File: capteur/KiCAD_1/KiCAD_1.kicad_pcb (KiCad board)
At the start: 2 copper layers, 68.6 x 58.3 mm, 25 parts, among them J1 Power, J2 Digital/PWM, J3 Analog, J4 Digital/PWM, U1 Bluetooth_HC05, U2 LTC1050CN8_PBF, U3 DM-OLED096-636, U4 Capteur_graphite, U5 Encodeur_Rotatif-KY-040, U6 Potentionmettre-MCP41010-I_P, U7 Flex_sensor, U8 Servomotor

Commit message: first change
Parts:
- U2: value LTC1050CN8_PBF -> LTC1050CN8
- U3: value DM-OLED096-636 -> DM_OLED_096_636
- U4: value Capteur_graphite -> Graphite_sensor
- U5: value Encodeur_Rotatif-KY-040 -> Rotary_encoder_KY_040
- U6: value Potentionmettre-MCP41010-I_P -> Potentionmettre_MCP41010
- moved U7 1.58 mm to (128.0, 89.0)
- moved U4 1.50 mm to (120.0, 89.0)
- moved R4 0.50 mm to (119.5, 83.5)
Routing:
- net VCC: track 189.1 -> 196.1 mm
- net Net-(U4-Output): track 12.3 -> 13.8 mm
- net SW: track 30.8 -> 32.2 mm
- net MOSI: track 53.2 -> 54.2 mm
- net PWM: track 46.5 -> 47.5 mm
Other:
- board size 68.6 x 58.3 mm -> 68.6 x 59.1 mm

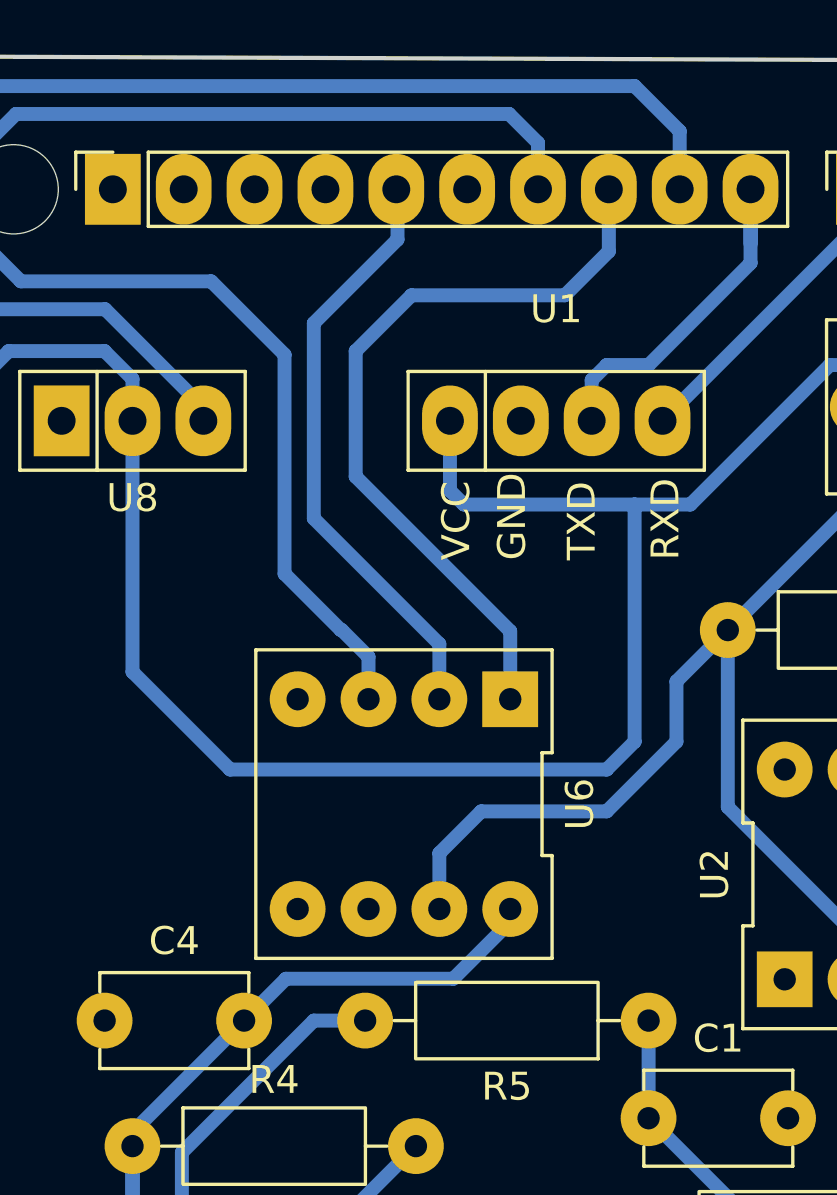
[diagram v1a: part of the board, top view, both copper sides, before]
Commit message: Added missing VCC connection
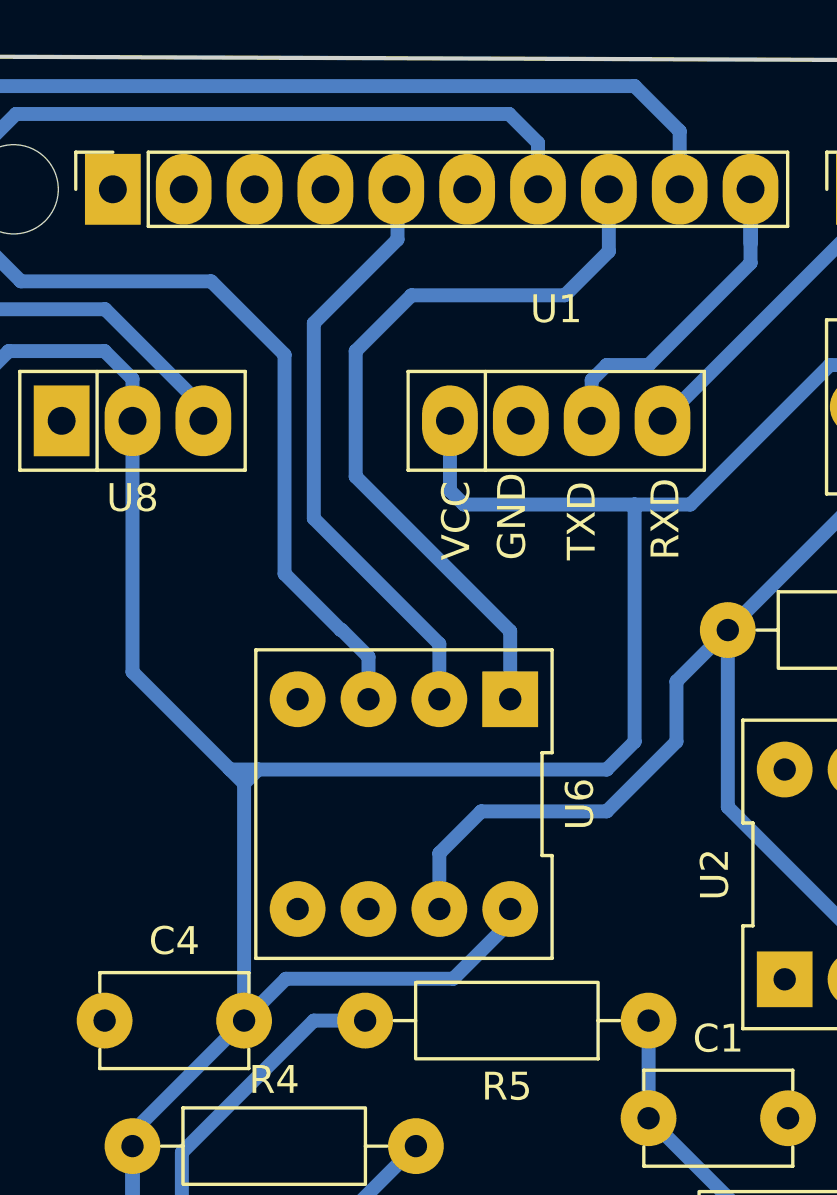
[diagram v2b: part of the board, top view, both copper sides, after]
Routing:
- net VCC: track 196.1 -> 206.0 mm
- net MOSI: track 54.2 -> 52.6 mm
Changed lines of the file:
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@@
-	)
-	(segment
-		(start 133.5 49.736)
-		(end 134.036 49.2)
-		(width 0.5)
-		(layer "B.Cu")
-		(net 7)
 	)
 	(segment
@@
 	)
 	(segment
-		(start 133.5 48.664)
-		(end 134.036 49.2)
-		(width 0.5)
-		(layer "B.Cu")
-		(net 7)
-	)
-	(segment
 		(start 127 65)
 		(end 126.968636 65)
@@
 	)
 	(segment
+		(start 123.5 70.5)
+		(end 124 70)
+		(width 0.5)
+		(layer "B.Cu")
+		(net 22)
+	)
+	(segment
 		(start 130.88 57.5)
 		(end 130.88 57.88)
@@
 	)
 	(segment
+		(start 123.5 70.5)
+		(end 123 70)
+		(width 0.5)
+		(layer "B.Cu")
+		(net 22)
+	)
+	(segment
 		(start 160.816 66.5)
 		(end 162 67.684)
@@
 	)
 	(segment
+		(start 124 70)
+		(end 123 70)
+		(width 0.5)
+		(layer "B.Cu")
+		(net 22)
+	)
+	(segment
 		(start 147.5 67.92)
 		(end 147.5 56.297787)
@@
 	(segment
 		(start 136.5 70)
-		(end 123 70)
+		(end 124 70)
 		(width 0.5)
 		(layer "B.Cu")
@@
 		(width 0.5)
 		(layer "B.Cu")
+		(net 22)
+	)
+	(segment
+		(start 123.5 79)
+		(end 123.5 70.5)
+		(width 0.5)
+		(layer "B.Cu")
